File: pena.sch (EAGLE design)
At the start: 35 parts

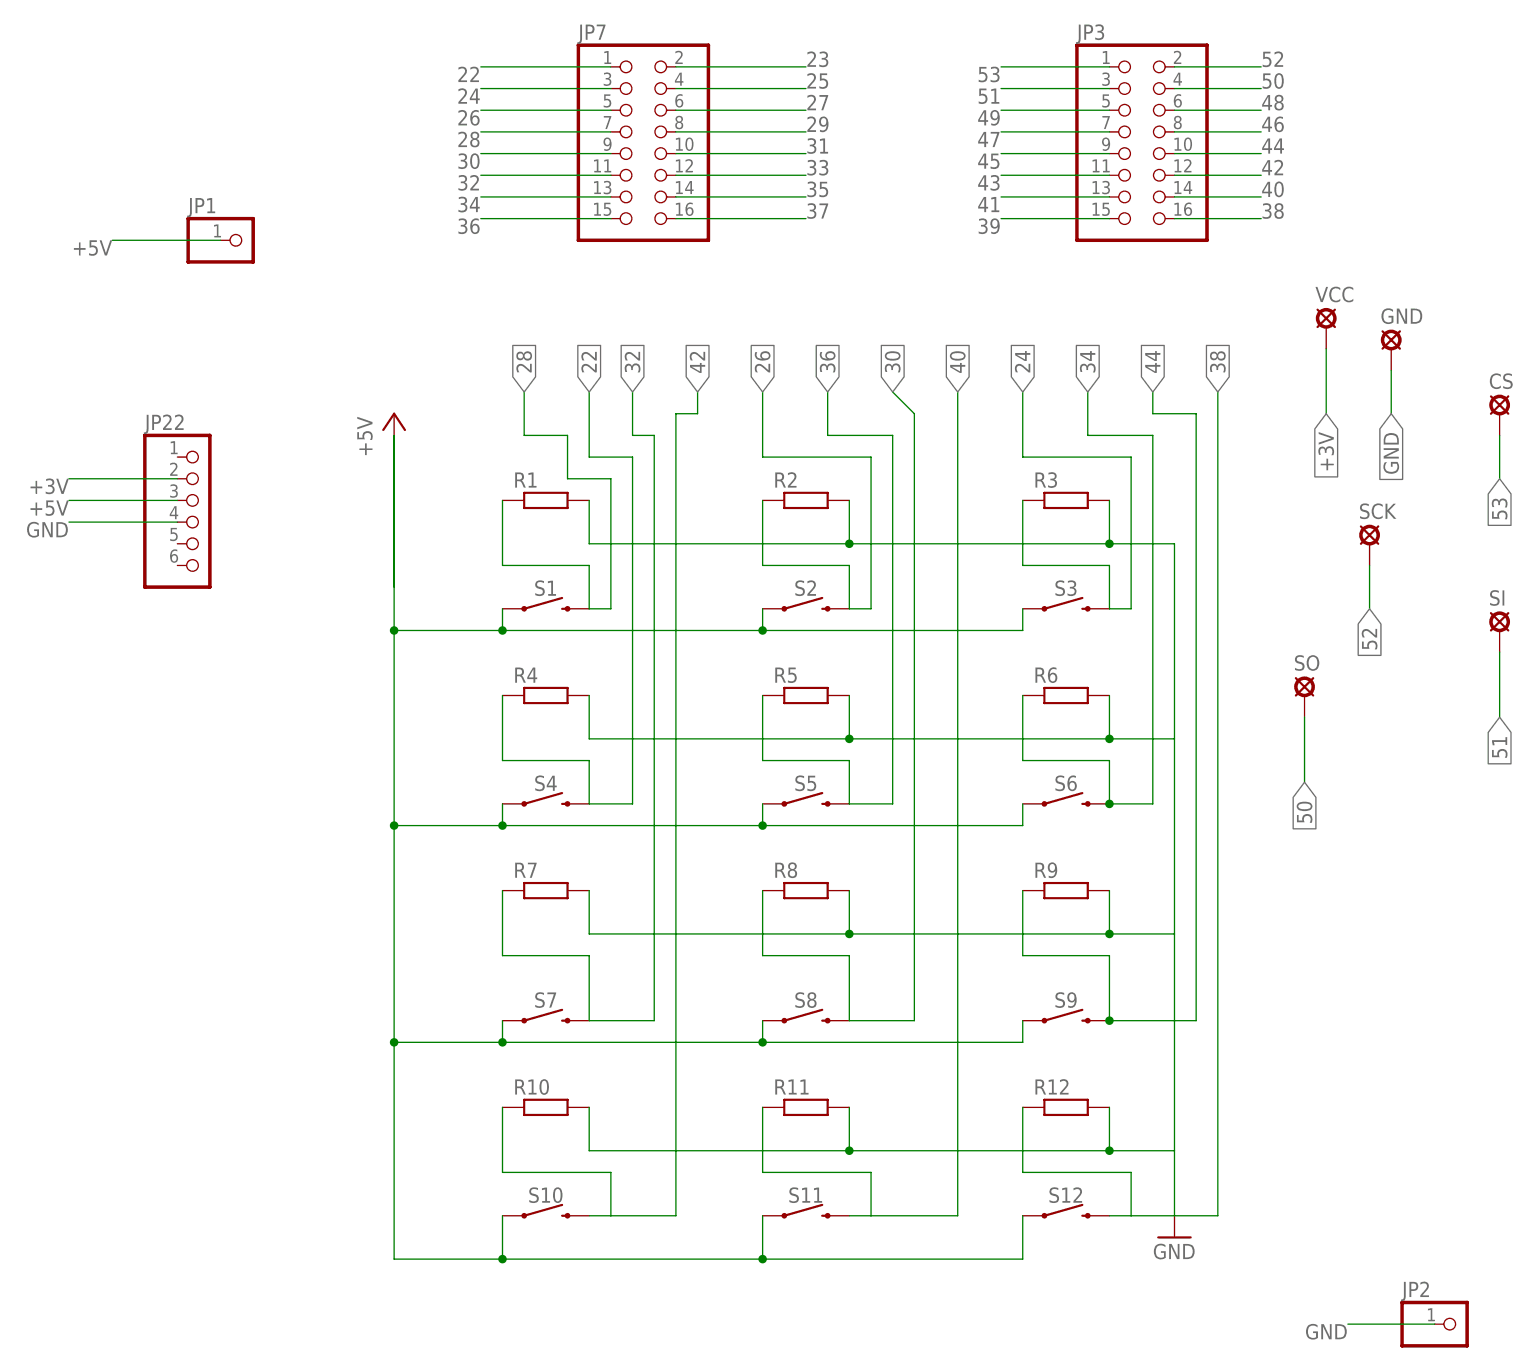
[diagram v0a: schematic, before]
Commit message: Muutettu boardin kokoa, reikien kokoa sekä poistettu alasveto vastukset.
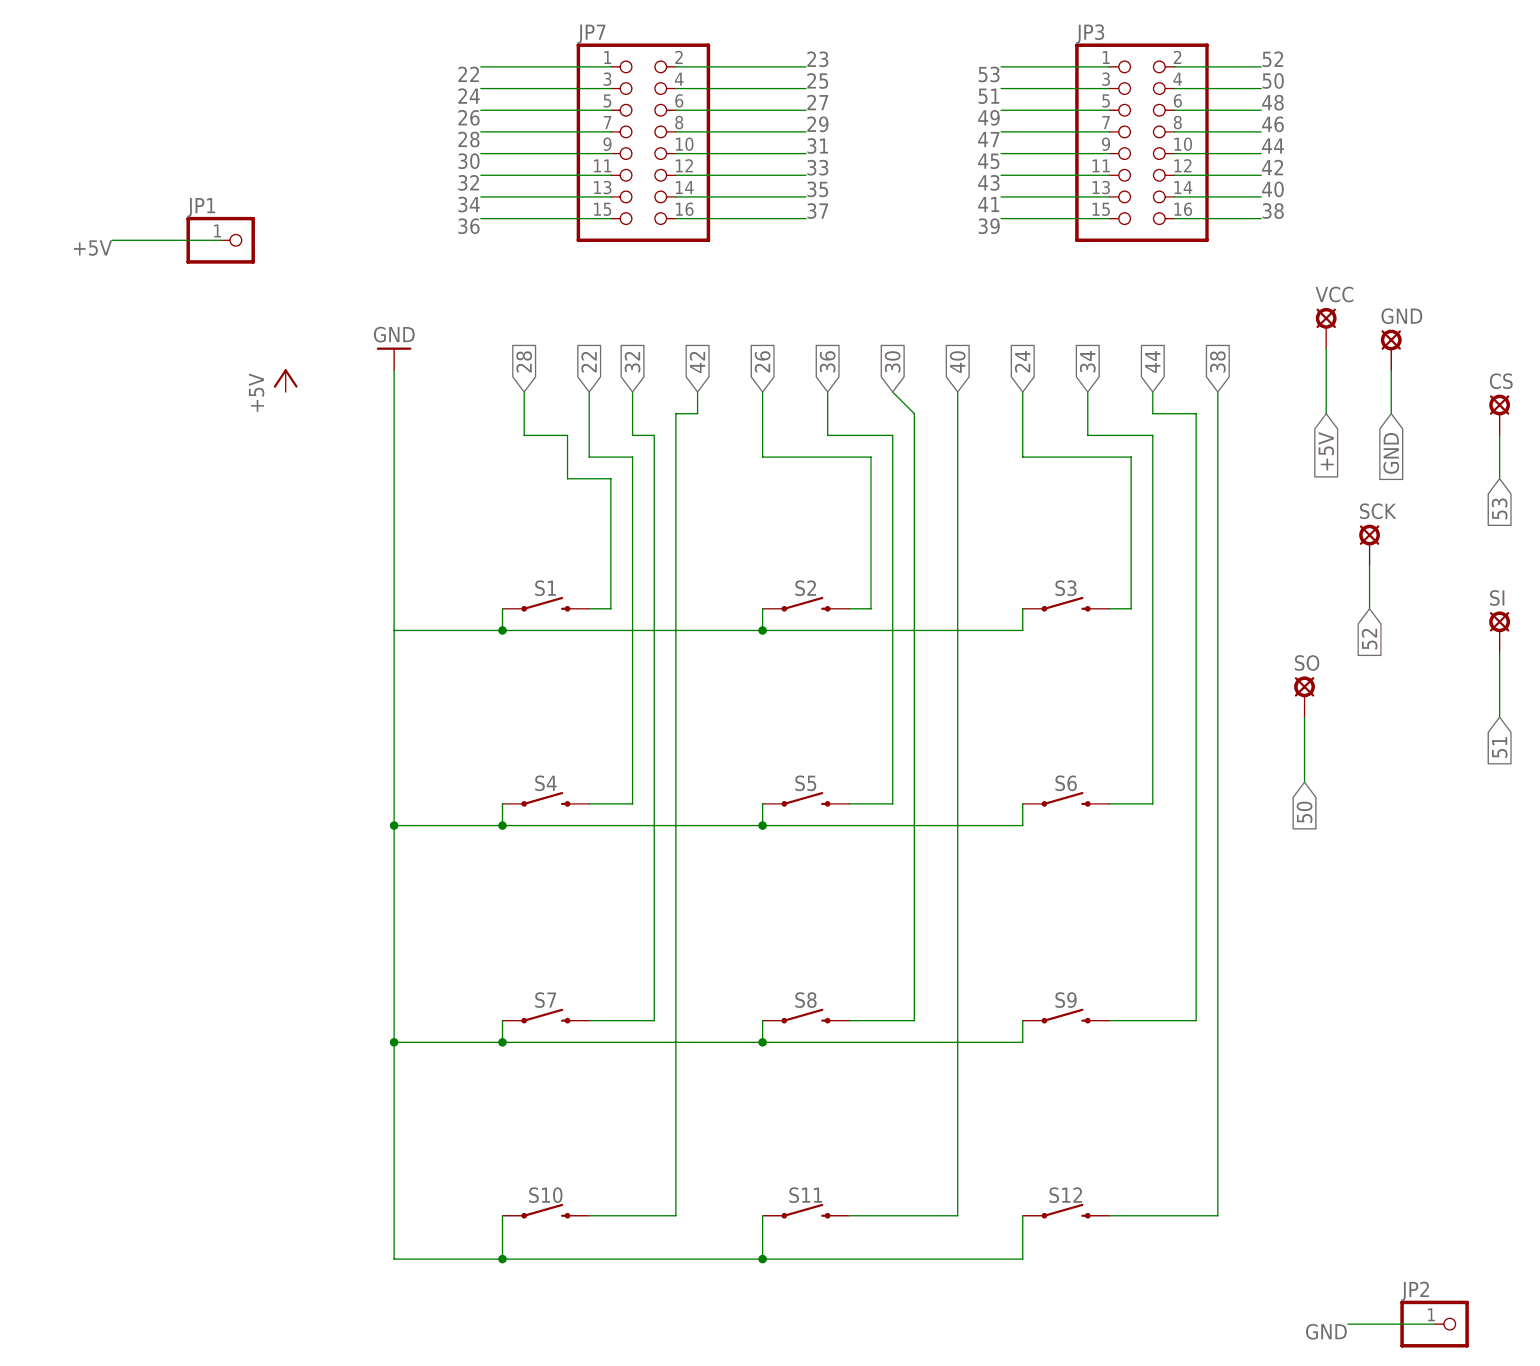
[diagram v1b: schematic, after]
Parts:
- removed JP22: (no value), mega:PINHD-1X6
- removed R1, R10, R11, R12, R2, R3, R4, R5, R6, R7, R8, R9: (no value), resistor:R-EU_0207/10
- CS, GND, SCK, SI, SO, VCC: value MCS10B -> SE14; device solpad:MCS10B -> solpad:SE14
- JP3: device mega:PINHD-2X8 -> pinhead:PINHD-2X8
- JP7: device pena:PINHD-2X8 -> pinhead:PINHD-2X8
- S1, S10, S11, S12, S2, S3, S4, S5, S6, S7, S8, S9: device mega:MOMENTARY-SWITCH-SPST-PTH-12MM -> SparkFun-Switches:MOMENTARY-SWITCH-SPST-PTH-12MM
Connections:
- removed net +3V: JP22.2, VCC.MP
- net +5V: now also VCC.MP; no longer JP22.3, S1.1, S10.1, S11.1, S12.1, S2.1, S3.1, S4.1, S5.1, S6.1, S7.1, S8.1, S9.1
- net 22: no longer R4.1
- net 24: no longer R3.1
- net 26: no longer R2.1
- net 28: no longer R1.1
- net 30: no longer R8.1
- net 32: no longer R7.1
- net 34: no longer R6.1
- net 36: no longer R5.1
- net 38: no longer R12.1
- net 40: no longer R11.1
- net 42: no longer R10.1
- net 44: no longer R9.1
- net GND: now also S1.1, S10.1, S11.1, S12.1, S2.1, S3.1, S4.1, S5.1, S6.1, S7.1, S8.1, S9.1; no longer JP22.4, R1.2, R10.2, R11.2, R12.2, R2.2, R3.2, R4.2, R5.2, R6.2, R7.2, R8.2, R9.2
